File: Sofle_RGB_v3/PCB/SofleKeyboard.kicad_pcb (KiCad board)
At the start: 2 copper layers, 143.4 x 111.8 mm, 96 parts, among them J1 LED, J2 4PIN, J3 OLED, P1 i2c_pin, P2 i2c_pin, SW1 SW_PUSH-MX_W_LED, SW10 SW_PUSH-MX_W_LED, SW11 SW_PUSH-MX_W_LED, SW12 SW_PUSH-MX_W_LED, SW13 SW_PUSH-MX_W_LED, SW14 SW_PUSH-MX_W_LED, SW15 SW_PUSH-MX_W_LED, SW16 SW_PUSH-MX_W_LED, SW17 SW_PUSH-MX_W_LED, SW18 SW_PUSH-MX_W_LED, SW19 SW_PUSH-MX_W_LED, SW2 SW_PUSH-MX_W_LED, SW20 SW_PUSH-MX_W_LED, SW21 SW_PUSH-MX_W_LED, SW22 SW_PUSH-MX_W_LED, SW23 SW_PUSH-MX_W_LED, SW24 SW_PUSH-MX_W_LED, SW25 Rotary_Encoder_Switch, SW26 SW_PUSH-MX_W_LED, SW27 SW_PUSH-MX_W_LED, SW28 SW_PUSH-MX_W_LED, SW29 SW_PUSH-MX_W_LED, SW3 SW_PUSH-MX_W_LED, SW30 SW_PUSH-MX_W_LED, SW4 SW_PUSH-MX_W_LED, SW5 SW_PUSH-MX_W_LED, SW6 SW_PUSH-MX_W_LED, SW7 SW_PUSH-MX_W_LED, SW8 SW_PUSH-MX_W_LED, SW9 SW_PUSH-MX_W_LED, U1 ProMicro

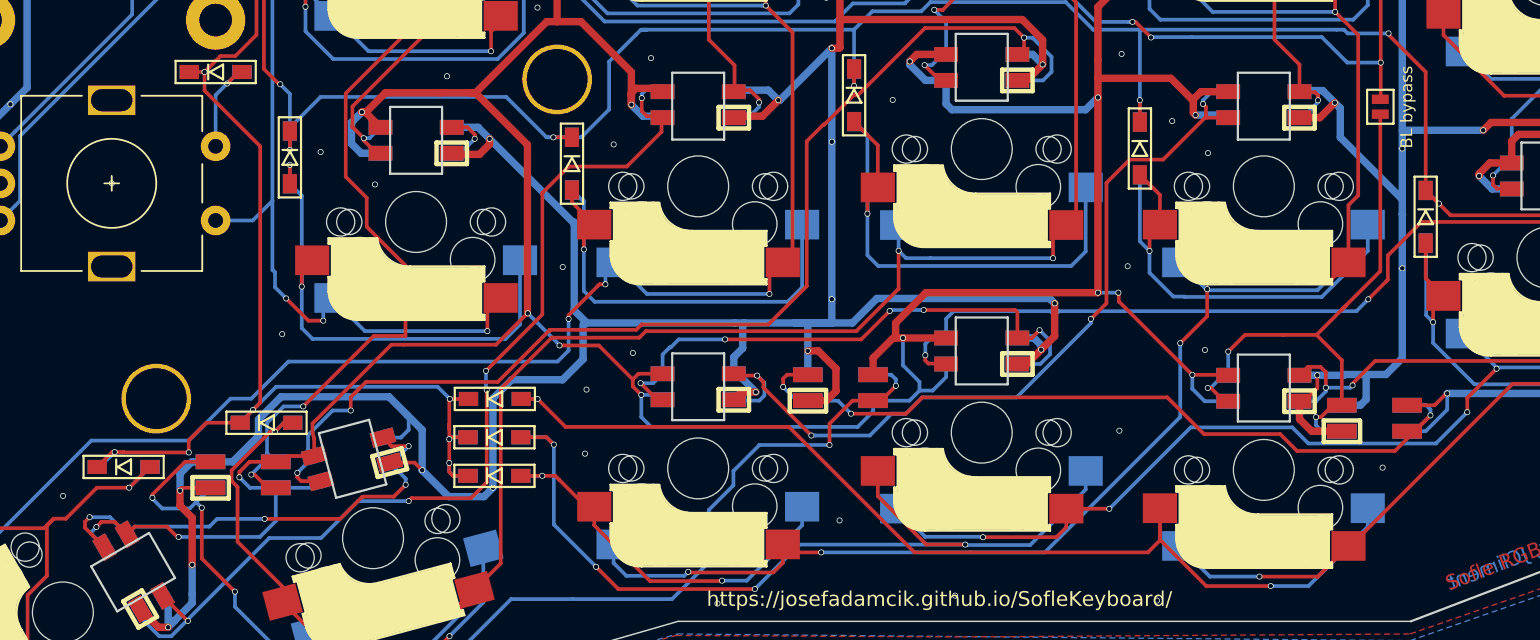
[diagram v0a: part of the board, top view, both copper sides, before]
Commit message: More fixes on GND/VCC tracks.
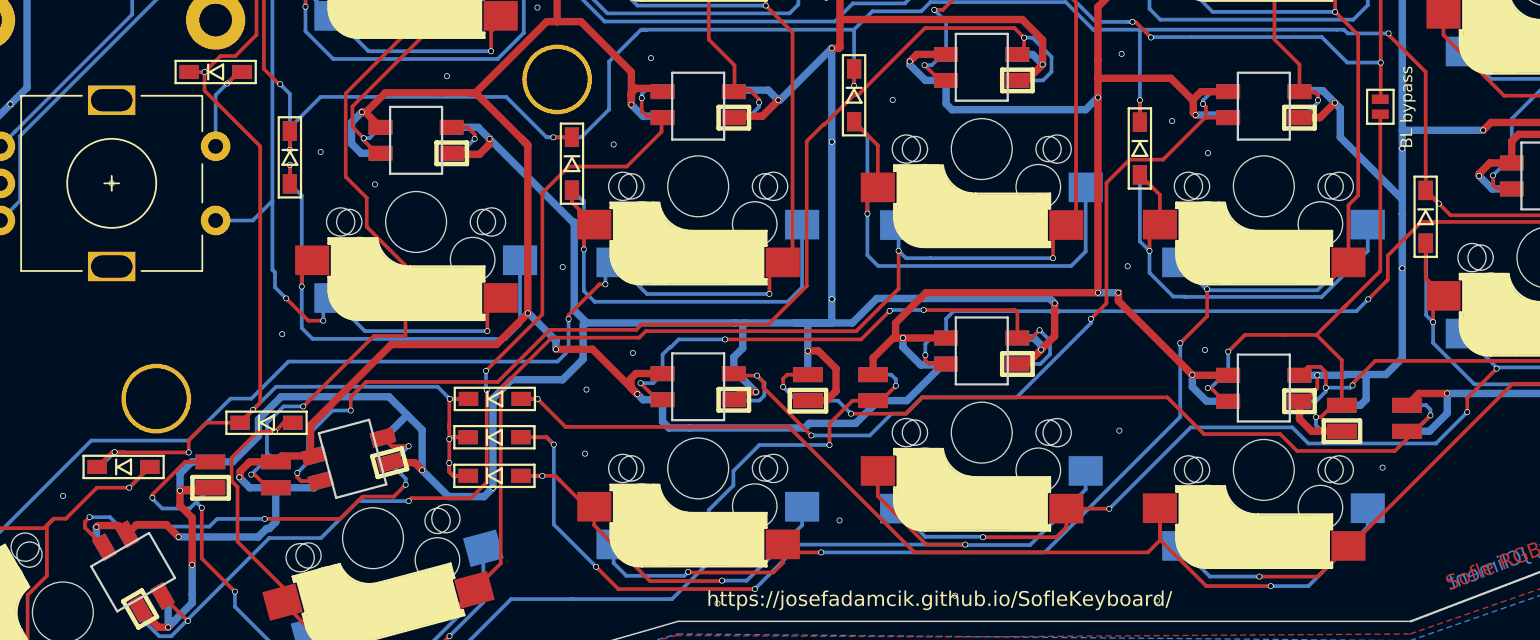
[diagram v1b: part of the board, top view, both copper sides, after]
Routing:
- net VCC: track 923.8 -> 927.3 mm
- net GND: track 994.9 -> 996.3 mm
